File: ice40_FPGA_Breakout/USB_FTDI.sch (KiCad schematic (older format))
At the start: 52 parts

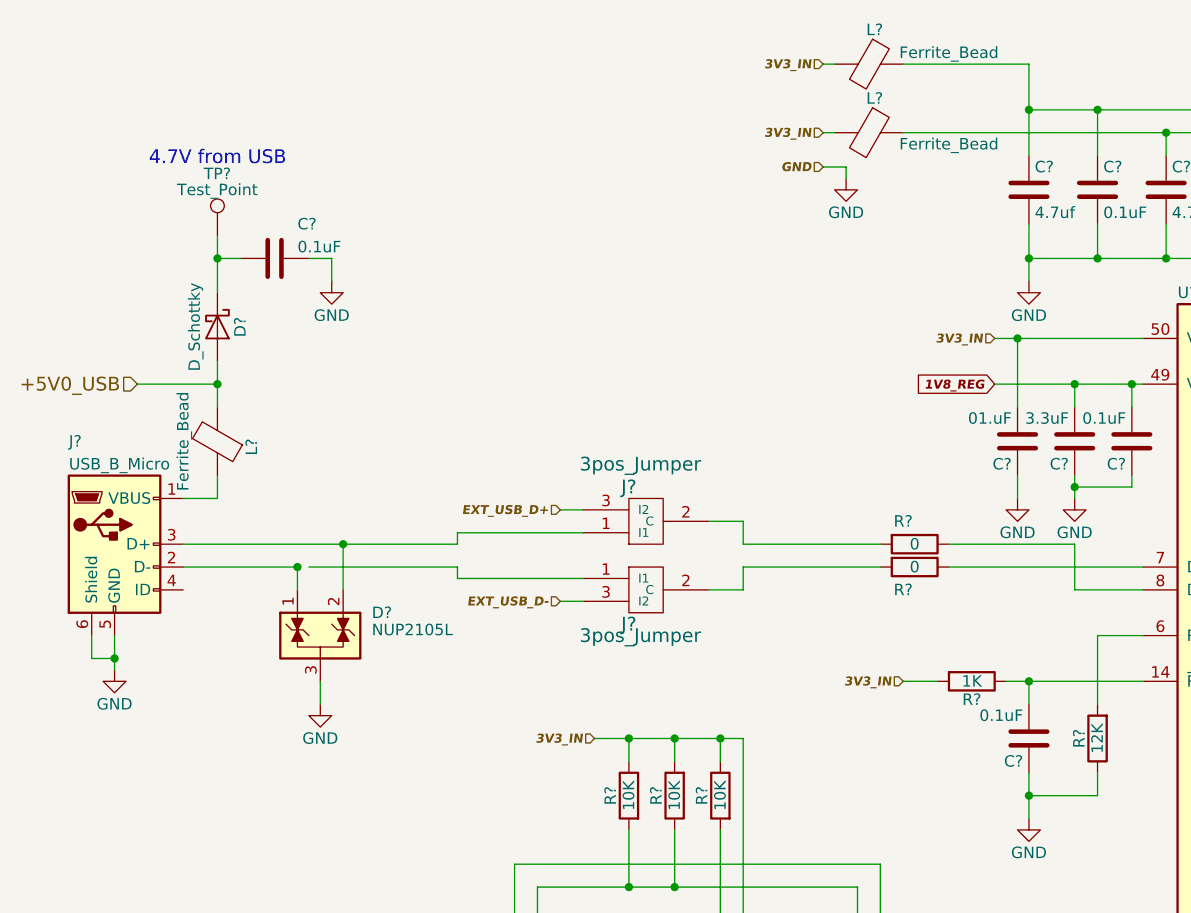
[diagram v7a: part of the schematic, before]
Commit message: fix based on feedback and decoupluing caps added
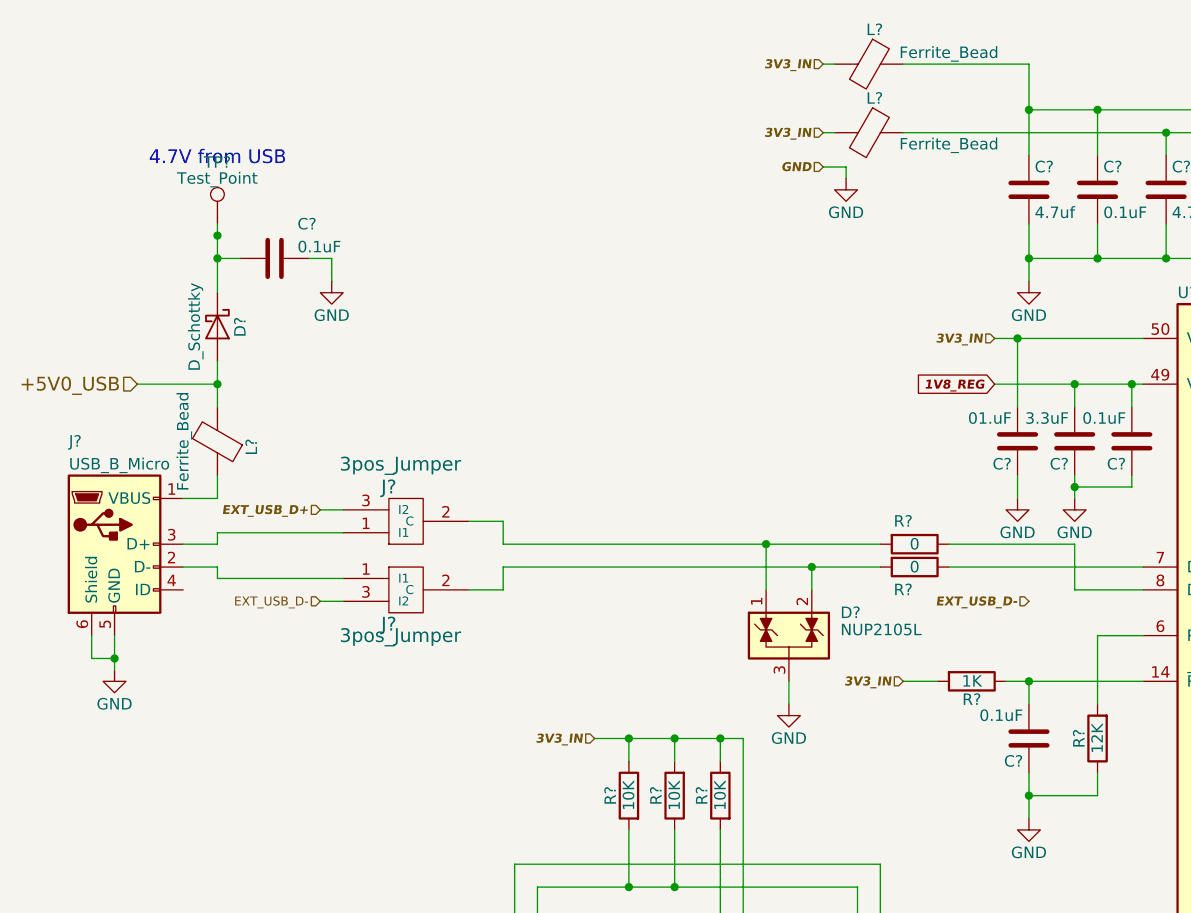
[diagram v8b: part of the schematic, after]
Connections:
- net at J?.2 (D-): now also J?.1 (I1); no longer D?.1 (K)
- net at J?.1 (I1), J?.3 (D+): no longer D?.2 (K)
- net at J?.2 (C), R?.2: now also D?.1 (K)
- net at J?.2 (C), R?.2: now also D?.2 (K)
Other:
- moved on the sheet: D?, J?, TP?
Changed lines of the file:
@@
 L NUP2105L D?
 U 1 1 5A0CEFF4
-P 2450 3150
-F 0 "D?" H 2675 3250 50  0000 L CNN
-F 1 "NUP2105L" H 2675 3175 50  0000 L CNN
-F 2 "TO_SOT_Packages_SMD:SOT-23" H 2675 3100 50  0001 L CNN
-F 3 "" H 2575 3275 50  0001 C CNN
-	1    2450 3150
+P 4500 3150
+F 0 "D?" H 4725 3250 50  0000 L CNN
+F 1 "NUP2105L" H 4725 3175 50  0000 L CNN
+F 2 "TO_SOT_Packages_SMD:SOT-23" H 4725 3100 50  0001 L CNN
+F 3 "" H 4625 3275 50  0001 C CNN
+	1    4500 3150
 	1    0    0    -1
 $EndComp
@@
 L GND #PWR026
 U 1 1 5A0D17DA
-P 2450 3450
-F 0 "#PWR026" H 2450 3200 50  0001 C CNN
-F 1 "GND" H 2450 3300 50  0000 C CNN
-F 2 "" H 2450 3450 50  0001 C CNN
-F 3 "" H 2450 3450 50  0001 C CNN
-	1    2450 3450
+P 4500 3450
+F 0 "#PWR026" H 4500 3200 50  0001 C CNN
+F 1 "GND" H 4500 3300 50  0000 C CNN
+F 2 "" H 4500 3450 50  0001 C CNN
+F 3 "" H 4500 3450 50  0001 C CNN
+	1    4500 3450
 	1    0    0    -1
 $EndComp
@@
 L 3pos_Jumper J?
 U 1 1 5A2C5B3A
-P 3850 2900
-F 0 "J?" H 3800 3100 60  0000 C CNN
-F 1 "3pos_Jumper" H 3850 3150 60  0000 C CNN
-F 2 "" H 3850 2900 60  0001 C CNN
-F 3 "" H 3850 2900 60  0001 C CNN
-	1    3850 2900
+P 2800 2900
+F 0 "J?" H 2750 3100 60  0000 C CNN
+F 1 "3pos_Jumper" H 2800 3150 60  0000 C CNN
+F 2 "" H 2800 2900 60  0001 C CNN
+F 3 "" H 2800 2900 60  0001 C CNN
+	1    2800 2900
 	1    0    0    1
 $EndComp
@@
 L 3pos_Jumper J?
 U 1 1 5A2C5C1B
-P 3850 2700
-F 0 "J?" H 3800 2900 60  0000 C CNN
-F 1 "3pos_Jumper" H 3850 3000 60  0000 C CNN
-F 2 "" H 3850 2700 60  0001 C CNN
-F 3 "" H 3850 2700 60  0001 C CNN
-	1    3850 2700
+P 2800 2700
+F 0 "J?" H 2750 2900 60  0000 C CNN
+F 1 "3pos_Jumper" H 2800 3000 60  0000 C CNN
+F 2 "" H 2800 2700 60  0001 C CNN
+F 3 "" H 2800 2700 60  0001 C CNN
+	1    2800 2700
 	1    0    0    -1
 $EndComp
@@
 L Test_Point TP?
 U 1 1 5A2FCE0A
-P 2000 1400
-F 0 "TP?" H 2000 1670 50  0000 C CNN
-F 1 "Test_Point" H 2000 1600 50  0000 C CNN
-F 2 "" H 2200 1400 50  0001 C CNN
-F 3 "" H 2200 1400 50  0001 C CNN
-	1    2000 1400
+P 2000 1350
+F 0 "TP?" H 2000 1620 50  0000 C CNN
+F 1 "Test_Point" H 2000 1550 50  0000 C CNN
+F 2 "" H 2200 1350 50  0001 C CNN
+F 3 "" H 2200 1350 50  0001 C CNN
+	1    2000 1350
 	1    0    0    -1
 $EndComp
@@
 Text HLabel 9150 2550 2    39   Input Italic 8
 FTDI_GPIO7
-Text HLabel 3500 2600 0    39   Input Italic 8
+Text HLabel 2450 2600 0    39   Input Italic 8
 EXT_USB_D+
-Text HLabel 3500 3000 0    39   Input Italic 8
+Text HLabel 5550 3000 0    39   Input Italic 8
 EXT_USB_D-
 Text HLabel 5400 1850 0    39   Input Italic 8
@@
 Connection ~ 7450 6050
 Wire Wire Line
-	2450 3350 2450 3450
-Wire Wire Line
-	2350 2850 2350 2950
-Wire Wire Line
-	2550 2750 2550 2950
+	4500 3350 4500 3450
 Wire Wire Line
 	5750 2950 6050 2950
-Connection ~ 2550 2750
-Connection ~ 2350 2850
 Wire Wire Line
 	1550 3150 1550 3300
@@
 	5200 2750 5750 2750
 Wire Wire Line
-	1850 2850 2350 2850
-Wire Wire Line
-	1850 2750 3050 2750
+	1850 2850 2000 2850
+Wire Wire Line
+	1850 2750 2000 2750
 Wire Wire Line
 	5450 3350 6050 3350
@@
 	2000 1950 2000 2150
 Wire Wire Line
-	2000 1400 2000 1650
+	2000 1350 2000 1650
 Wire Wire Line
 	1850 2550 2000 2550
@@
 Connection ~ 5250 5600
 Wire Wire Line
-	3050 2750 3050 2700
-Wire Wire Line
-	3050 2700 3600 2700
-Wire Wire Line
-	2400 2850 3050 2850
-Wire Wire Line
-	3050 2850 3050 2900
-Wire Wire Line
-	3050 2900 3600 2900
-Wire Wire Line
-	4150 2650 4300 2650
-Wire Wire Line
-	4300 2650 4300 2750
-Wire Wire Line
-	4300 2750 4900 2750
-Wire Wire Line
-	4150 2950 4300 2950
-Wire Wire Line
-	4300 2950 4300 2850
-Wire Wire Line
-	4300 2850 4900 2850
-Wire Wire Line
-	3600 2600 3500 2600
-Wire Wire Line
-	3600 3000 3500 3000
+	2000 2750 2000 2700
+Wire Wire Line
+	2000 2700 2550 2700
+Wire Wire Line
+	2000 2850 2000 2900
+Wire Wire Line
+	2000 2900 2550 2900
+Wire Wire Line
+	3100 2650 3250 2650
+Wire Wire Line
+	3250 2650 3250 2750
+Wire Wire Line
+	3250 2750 4900 2750
+Wire Wire Line
+	3100 2950 3250 2950
+Wire Wire Line
+	3250 2950 3250 2850
+Wire Wire Line
+	3250 2850 4900 2850
+Wire Wire Line
+	2550 2600 2450 2600
+Wire Wire Line
+	2450 3000 2550 3000
 Wire Wire Line
 	4100 4850 4300 4850
@@
 Text HLabel 1650 2050 0    60   Input ~ 0
 +5V0_USB
+Text HLabel 2450 3000 0    39   Input ~ 0
+EXT_USB_D-
+Wire Wire Line
+	4400 2950 4400 2750
+Connection ~ 4400 2750
+Wire Wire Line
+	4600 2950 4600 2850
+Connection ~ 4600 2850
+Connection ~ 2000 1400
 $EndSCHEMATC
